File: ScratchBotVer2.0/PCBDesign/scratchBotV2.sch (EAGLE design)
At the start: 38 parts, among them T1 BD139, T3 BD139

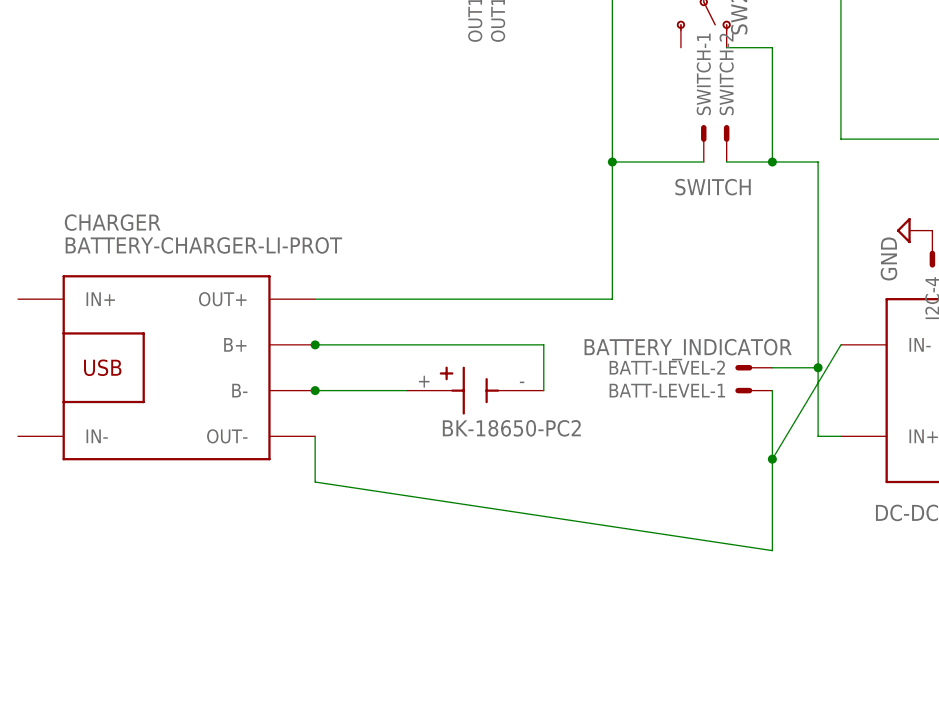
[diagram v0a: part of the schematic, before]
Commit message: Li ion battery added and review of other components mentioned in the FRD
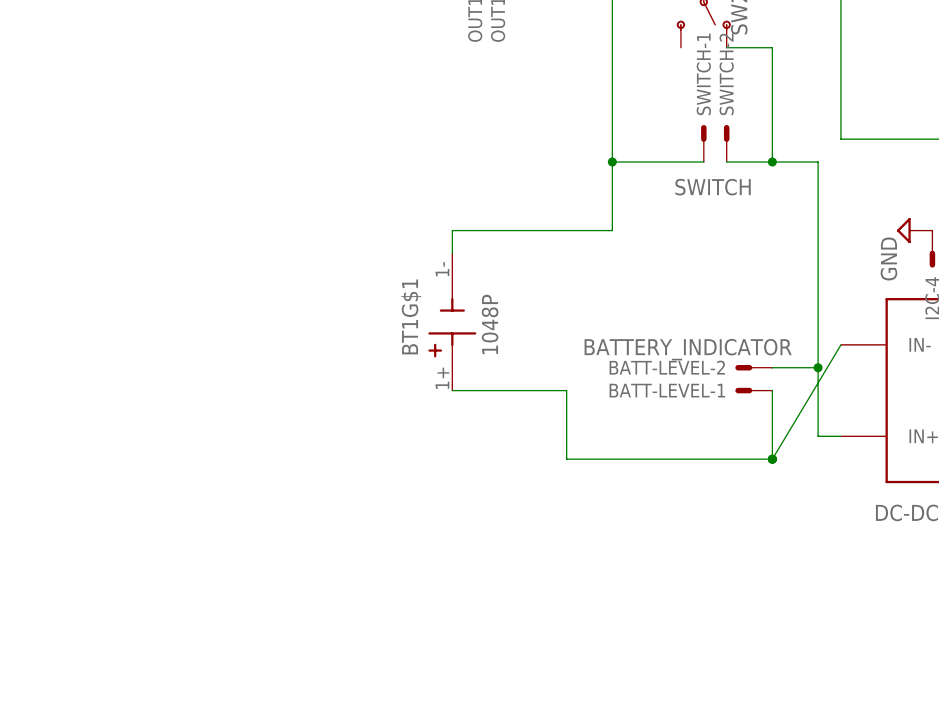
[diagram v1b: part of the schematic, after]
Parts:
- removed CHARGER: BATTERY-CHARGER-LI-PROT, diy-modules:BATTERY-CHARGER-LI-PROT
- removed LI-IONBATTERY: BK-18650-PC2, BK-18650-PC2:BK-18650-PC2
- added BT1: 1048P, 1048P:1048P
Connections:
- removed net N$3: CHARGER.B+, LI-IONBATTERY.-
- removed net N$32: CHARGER.OUT+, SW2.P, SWITCH-1.S
- net N$1: now also BT1G$1.1-, SW2.P, SWITCH-1.S; no longer CHARGER.B-, LI-IONBATTERY.+
- net N$6: now also BT1G$1.1+; no longer CHARGER.OUT-
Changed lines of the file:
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@@
 <part name="DRIVER" library="st-microelectronics" library_urn="urn:adsk.eagle:library:368" deviceset="L293D" device="" package3d_urn="urn:adsk.eagle:package:26820/1"/>
 <part name="BOOSTER" library="diy-modules" deviceset="DC-DC-STEP-UP-MT3608" device=""/>
-<part name="CHARGER" library="diy-modules" deviceset="BATTERY-CHARGER-LI-PROT" device=""/>
-<part name="LI-IONBATTERY" library="BK-18650-PC2" deviceset="BK-18650-PC2" device=""/>
 <part name="SUPPLY1" library="supply2" library_urn="urn:adsk.eagle:library:372" deviceset="GND" device=""/>
 <part name="SUPPLY2" library="supply2" library_urn="urn:adsk.eagle:library:372" deviceset="GND" device=""/>
@@
 <part name="SUPPLY31" library="supply2" library_urn="urn:adsk.eagle:library:372" deviceset="GND" device=""/>
 <part name="3.3V" library="SparkFun-Connectors" deviceset="CONN_02" device=""/>
+<part name="BT1" library="1048P" deviceset="1048P" device=""/>
 </parts>
 <sheets>
@@
 <attribute name="VALUE" x="33.02" y="20.32" size="1.778" layer="96" rot="R180"/>
 </instance>
-<instance part="CHARGER" gate="G$1" x="-71.12" y="35.56" smashed="yes">
-<attribute name="NAME" x="-83.82" y="50.8" size="1.778" layer="95"/>
-<attribute name="VALUE" x="-83.82" y="48.26" size="1.778" layer="96"/>
-</instance>
-<instance part="LI-IONBATTERY" gate="G$1" x="-38.1" y="33.02" smashed="yes">
-<attribute name="VALUE" x="-41.91" y="27.94" size="1.778" layer="96"/>
-</instance>
 <instance part="SUPPLY1" gate="GND" x="48.26" y="35.56" smashed="yes">
 <attribute name="VALUE" x="46.355" y="32.385" size="1.778" layer="96"/>
@@
 <attribute name="VALUE" x="132.08" y="147.066" size="1.778" layer="96" font="vector" rot="R180"/>
 <attribute name="NAME" x="132.08" y="136.652" size="1.778" layer="95" font="vector" rot="R180"/>
+</instance>
+<instance part="BT1" gate="G$1" x="-40.64" y="40.64" smashed="yes" rot="R90">
+<attribute name="NAME" x="-44.45" y="36.83" size="1.778" layer="95" rot="R90"/>
+<attribute name="VALUE" x="-35.56" y="36.83" size="1.778" layer="96" rot="R90"/>
 </instance>
 </instances>
@@
 </segment>
 </net>
-<net name="N$1" class="0">
-<segment>
-<pinref part="CHARGER" gate="G$1" pin="B-"/>
-<wire x1="-55.88" y1="33.02" x2="-45.72" y2="33.02" width="0.1524" layer="91"/>
-<junction x="-55.88" y="33.02"/>
-<pinref part="LI-IONBATTERY" gate="G$1" pin="+"/>
-</segment>
-</net>
-<net name="N$3" class="0">
-<segment>
-<pinref part="CHARGER" gate="G$1" pin="B+"/>
-<wire x1="-55.88" y1="38.1" x2="-30.48" y2="38.1" width="0.1524" layer="91"/>
-<wire x1="-30.48" y1="38.1" x2="-30.48" y2="33.02" width="0.1524" layer="91"/>
-<junction x="-55.88" y="38.1"/>
-<pinref part="LI-IONBATTERY" gate="G$1" pin="-"/>
-</segment>
-</net>
 <net name="N$6" class="0">
 <segment>
-<pinref part="CHARGER" gate="G$1" pin="OUT-"/>
-<wire x1="-55.88" y1="27.94" x2="-55.88" y2="22.86" width="0.1524" layer="91"/>
-<wire x1="-55.88" y1="22.86" x2="-5.08" y2="15.24" width="0.1524" layer="91"/>
 <pinref part="BOOSTER" gate="G$1" pin="IN-"/>
-<wire x1="-5.08" y1="15.24" x2="-5.08" y2="25.4" width="0.1524" layer="91"/>
 <wire x1="-5.08" y1="25.4" x2="2.54" y2="38.1" width="0.1524" layer="91"/>
 <wire x1="-5.08" y1="33.02" x2="-5.08" y2="25.4" width="0.1524" layer="91"/>
 <junction x="-5.08" y="25.4"/>
 <pinref part="BATT-LEVEL" gate="-1" pin="S"/>
+<wire x1="-5.08" y1="25.4" x2="-27.94" y2="25.4" width="0.1524" layer="91"/>
+<wire x1="-27.94" y1="25.4" x2="-27.94" y2="33.02" width="0.1524" layer="91"/>
+<junction x="-5.08" y="25.4"/>
+<pinref part="BT1" gate="G$1" pin="1+"/>
+<wire x1="-40.64" y1="33.02" x2="-27.94" y2="33.02" width="0.1524" layer="91"/>
 </segment>
 </net>
@@
 </segment>
 </net>
-<net name="N$32" class="0">
-<segment>
-<pinref part="SW2" gate="1" pin="P"/>
-<pinref part="CHARGER" gate="G$1" pin="OUT+"/>
-<wire x1="-55.88" y1="43.18" x2="-22.86" y2="43.18" width="0.1524" layer="91"/>
-<wire x1="-22.86" y1="43.18" x2="-22.86" y2="58.42" width="0.1524" layer="91"/>
-<wire x1="-22.86" y1="58.42" x2="-12.7" y2="58.42" width="0.1524" layer="91"/>
-<pinref part="SWITCH" gate="-1" pin="S"/>
-<wire x1="-12.7" y1="78.74" x2="-22.86" y2="78.74" width="0.1524" layer="91"/>
-<wire x1="-22.86" y1="78.74" x2="-22.86" y2="58.42" width="0.1524" layer="91"/>
-<junction x="-22.86" y="58.42"/>
-</segment>
-</net>
 <net name="N$33" class="0">
 <segment>
@@
 </segment>
 </net>
+<net name="N$1" class="0">
+<segment>
+<wire x1="-40.64" y1="50.8" x2="-22.86" y2="50.8" width="0.1524" layer="91"/>
+<pinref part="BT1" gate="G$1" pin="1-"/>
+<wire x1="-40.64" y1="48.26" x2="-40.64" y2="50.8" width="0.1524" layer="91"/>
+<pinref part="SW2" gate="1" pin="P"/>
+<wire x1="-22.86" y1="58.42" x2="-12.7" y2="58.42" width="0.1524" layer="91"/>
+<pinref part="SWITCH" gate="-1" pin="S"/>
+<wire x1="-12.7" y1="78.74" x2="-22.86" y2="78.74" width="0.1524" layer="91"/>
+<wire x1="-22.86" y1="78.74" x2="-22.86" y2="58.42" width="0.1524" layer="91"/>
+<wire x1="-22.86" y1="50.8" x2="-22.86" y2="58.42" width="0.1524" layer="91"/>
+<junction x="-22.86" y="58.42"/>
+</segment>
+</net>

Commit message: updated
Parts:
- removed BOOSTER: DC-DC-STEP-UP-MT3608, diy-modules:DC-DC-STEP-UP-MT3608
- added LDR: JST-XH-02-PIN-LONG-PAD, Rembrandt Electronics - JST XH Connectors v1-0:JST-XH-02-PIN-LONG-PAD
- added LED1: (no value), adafruit:LEDCHIPLED_1206
- added R1: 10K, bourns:3362H
- added R3: (no value), bourns:3362H
- added R4, R6, R7: 10K, adafruit:R-US_M1206
- added R5: (no value), adafruit:R-US_M1206
- added SERVO: SERVO, Rembrandt Electronics - JST XH Connectors v1-0 (1):JST-XH-03-PIN-LONG-PAD
- added T2, T4, T5: (no value), transistor:-NPN-SOT23-EBC
- added U1, U2: LM358M/NOPB, LM358M_NOPB:LM358M/NOPB
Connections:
- new net N$26: LDR-1.S, R4.2
- new net N$27: R6.1, U1.OUTA
- new net N$3: R1.2, U1.-INA
- new net N$31: R6.2, T2.B
- new net N$32: LED1.C, T2.C
- new net N$38: LED1.A, R7.1
- net 9V-MT3608: no longer BOOSTER.OUT+
- net GND: now also R1.1, R4.1, T2.E, U1.GND; no longer BOOSTER.OUT-
- net N$18: no longer BOOSTER.IN+
- net N$6: no longer BOOSTER.IN-
- net VCC: now also LDR-2.S, R1.3, R7.2, U1.V+

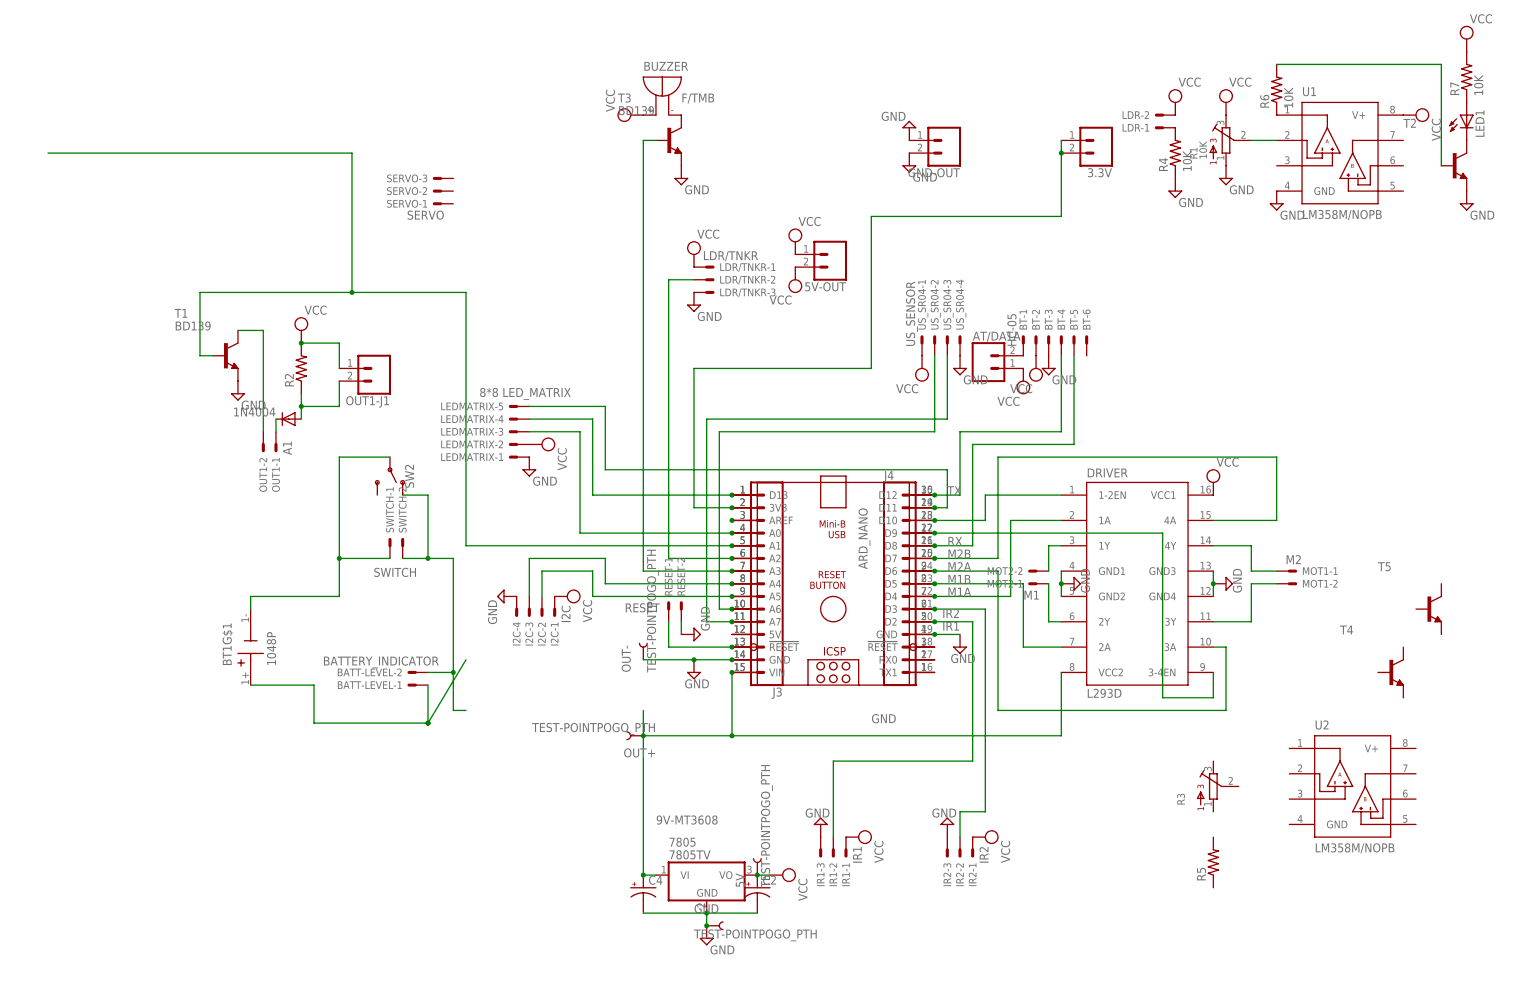
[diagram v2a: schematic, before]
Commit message: updated pin number
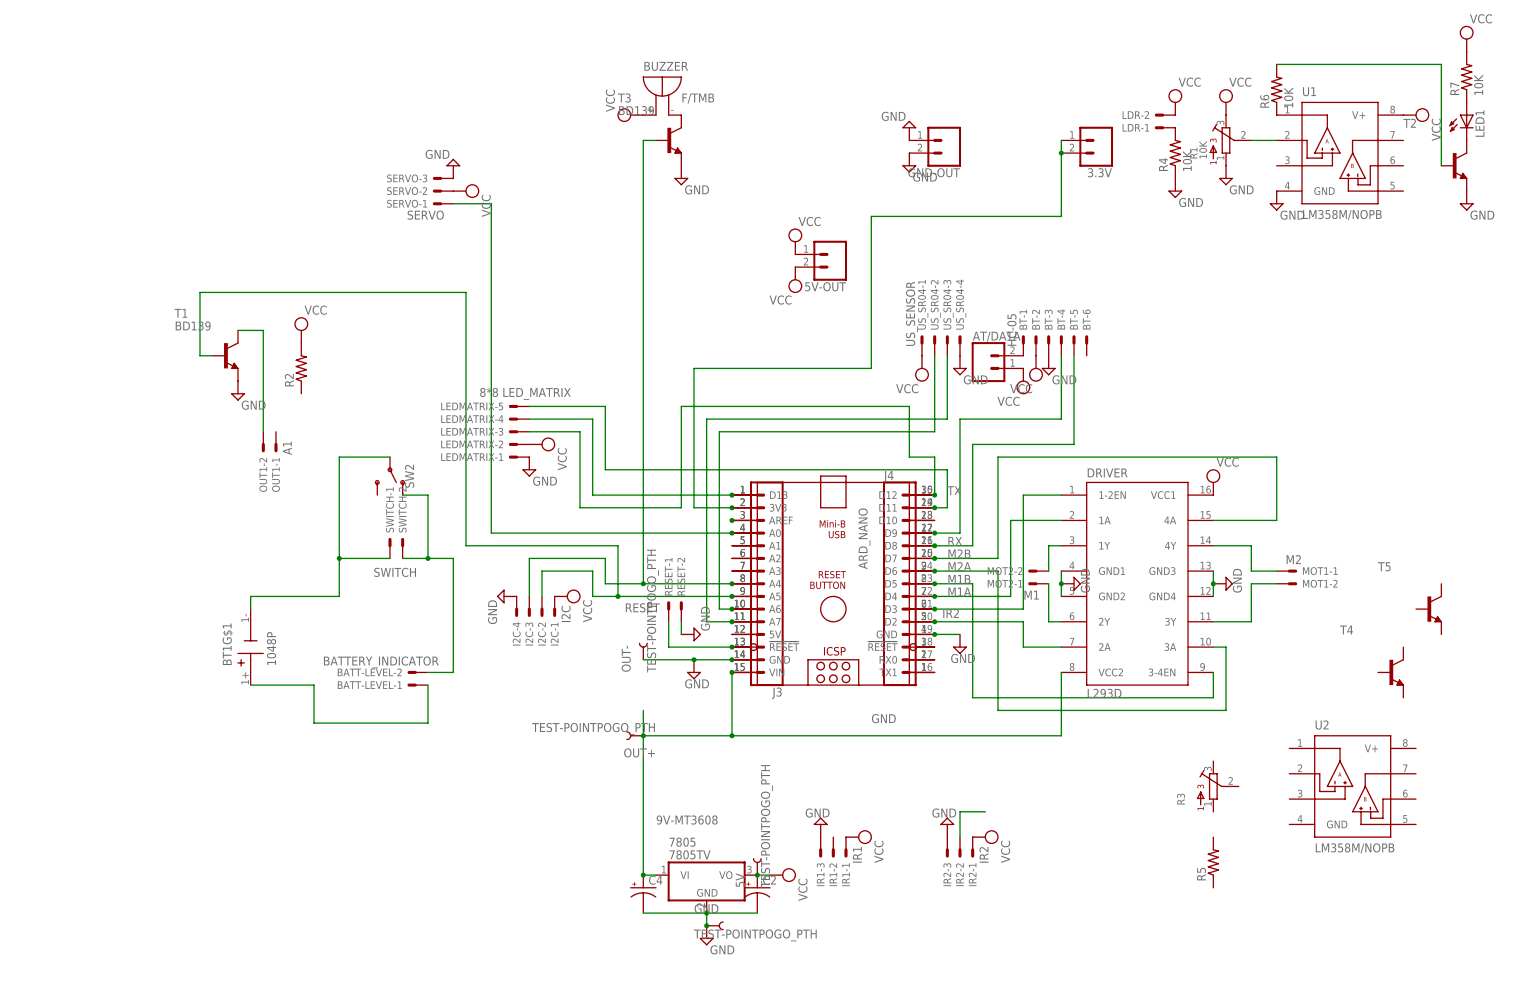
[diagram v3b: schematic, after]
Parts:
- removed D1: 1N4004, adafruit:1N4004
- removed LDR/TNKR: LDR/TNKR, Rembrandt Electronics - JST XH Connectors v1-0 (1):JST-XH-03-PIN-LONG-PAD
- removed OUT1-J1: (no value), SparkFun-Connectors:CONN_02
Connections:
- removed net IR1: ARD_NANO.D2, IR1-2.S, J4.5
- removed net N$24: ARD_NANO.A2, J3.6, LDR/TNKR-2.S
- removed net N$28: D1.A, OUT1-J1.2, R2.1
- removed net N$30: D1.C, OUT1-1.S
- new net N$39: ARD_NANO.D2, DRIVER.2A, J4.5
- new net N$40: IR2-2.S
- new net N$41: ARD_NANO.A3, J3.7
- net ECHO: now also ARD_NANO.A4, I2C-3.S, J3.8; no longer ARD_NANO.A3, J3.7
- net GND: now also SERVO-3.S; no longer LDR/TNKR-3.S
- net IR2: now also DRIVER.1-2EN; no longer IR2-2.S
- net M1B: now also DRIVER.3-4EN; no longer DRIVER.2A
- net N$10: no longer DRIVER.1-2EN
- net N$13: now also BT-4.S; no longer DRIVER.3-4EN
- net N$15: now also ARD_NANO.A1, J3.5; no longer ARD_NANO.A4, I2C-3.S, J3.8
- net N$16: now also ARD_NANO.A2, J3.6; no longer ARD_NANO.A5, I2C-2.S, J3.9
- net N$23: now also ARD_NANO.A5, I2C-2.S, J3.9; no longer ARD_NANO.A1, J3.5
- net N$5: now also SERVO-1.S; no longer LEDMATRIX-3.S
- net TX: now also LEDMATRIX-3.S; no longer BT-4.S
- net VCC: now also SERVO-2.S; no longer LDR/TNKR-1.S, OUT1-J1.1

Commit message: Two TCR5000  circuit added for line follower.
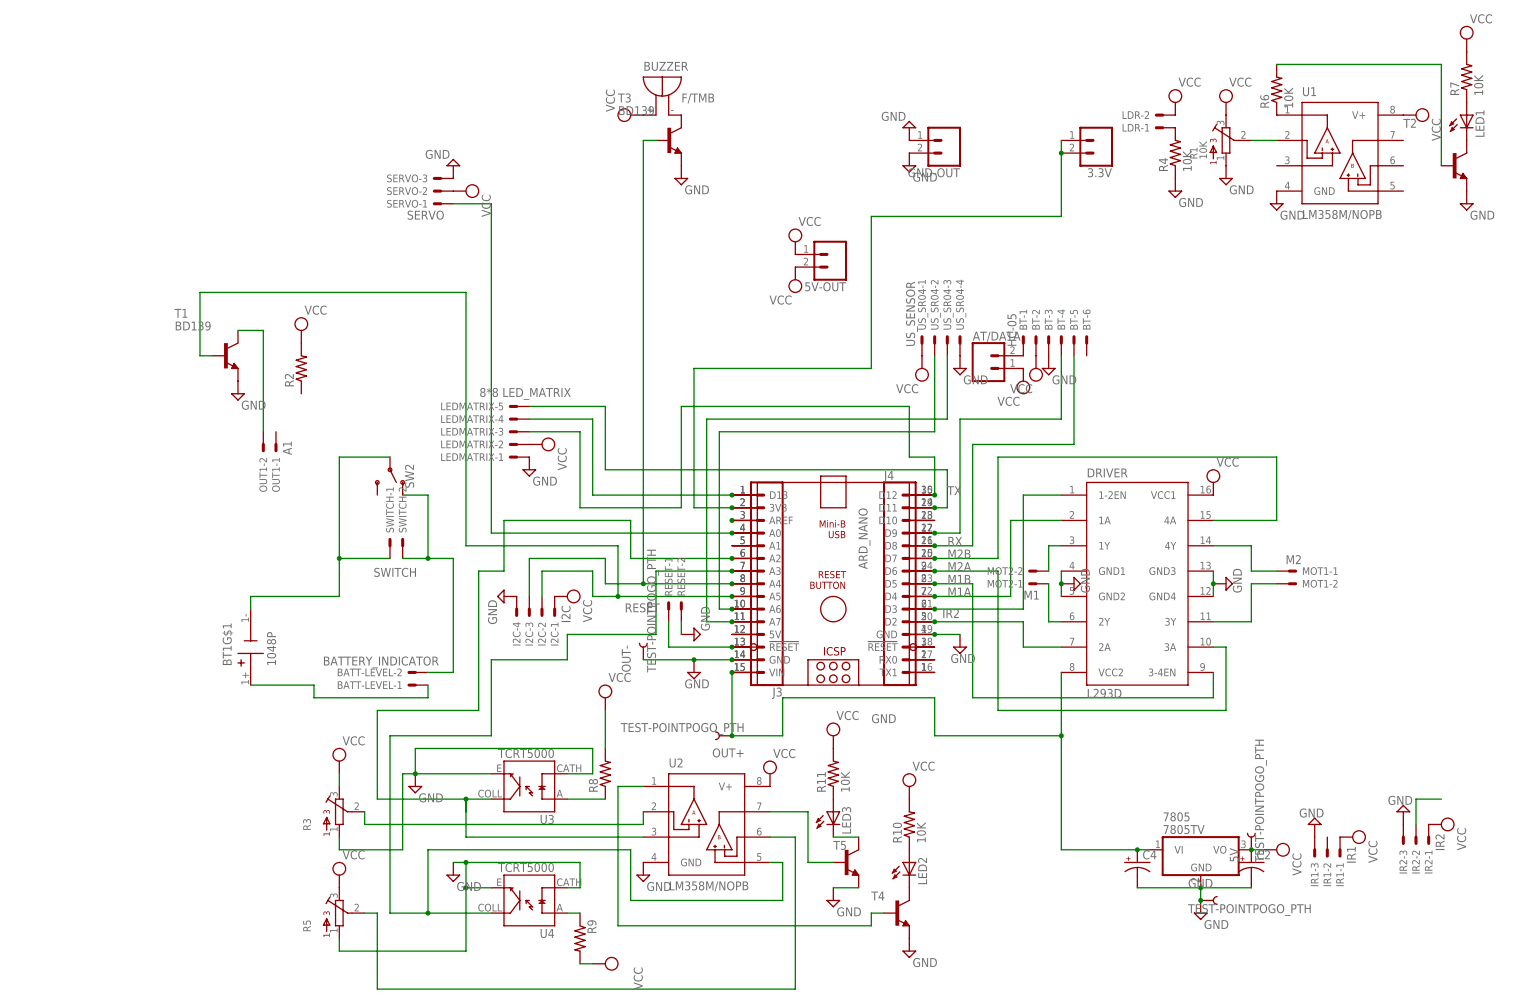
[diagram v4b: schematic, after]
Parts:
- added LED2, LED3: (no value), adafruit:LEDCHIPLED_1206
- added R10, R11: 10K, adafruit:R-US_M1206
- added R8, R9: (no value), adafruit:R-US_M1206
- added U3, U4: TCRT5000, TCRT5000:TCRT5000
- R5: device adafruit:R-US_M1206 -> bourns:3362H
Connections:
- new net N$24: R8.1, U3.A
- new net N$28: R9.1, U4.A
- new net N$30: LED2.C, T4.C
- new net N$42: R3.2, U2.-INA
- new net N$43: LED3.A, R11.1
- new net N$44: LED2.A, R10.1
- new net N$45: T4.B, U2.OUTA
- new net N$46: LED3.C, T5.C
- new net N$47: T5.B, U2.OUTB
- new net N$48: R5.2, U2.-INB
- net GND: now also R3.1, R5.1, T4.E, T5.E, U2.GND, U3.CATH, U3.E, U4.CATH, U4.E
- net N$16: now also U2.+INA, U3.COLL
- net N$41: now also U2.+INB, U4.COLL
- net VCC: now also R10.2, R11.2, R3.3, R5.3, R8.2, R9.2, U2.V+
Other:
- moved on the sheet: 5V, 7805, C2, C4, GND, IR1-1, IR1-2, IR1-3, IR2-1, IR2-2, IR2-3, OUT+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
